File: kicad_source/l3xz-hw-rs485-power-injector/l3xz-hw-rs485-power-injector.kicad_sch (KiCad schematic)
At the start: 24 parts, among them J1 PowerPole, J2 Conn_01x02, J3 Conn_01x03, J4 SM04B-GHS-TB, J5 EH_S4B-EH, J6 EH_S4B-EH, J7 Conn_01x04, U1 L78L05_SOT89, U2 SN75176AD

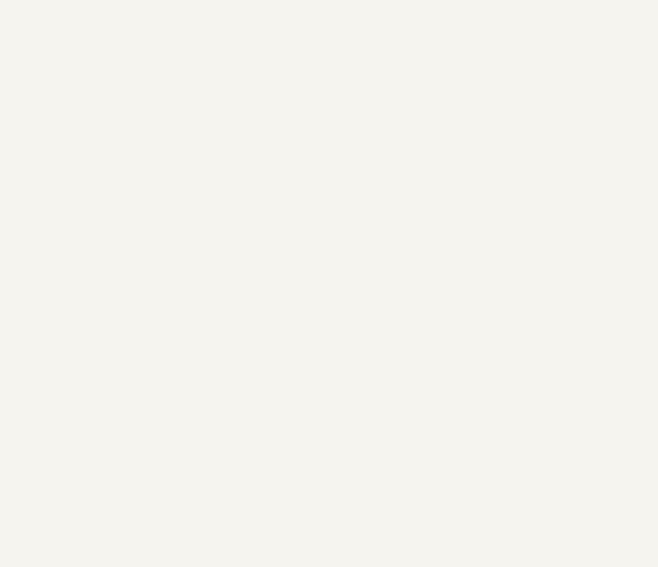
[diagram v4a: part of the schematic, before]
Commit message: added some labels
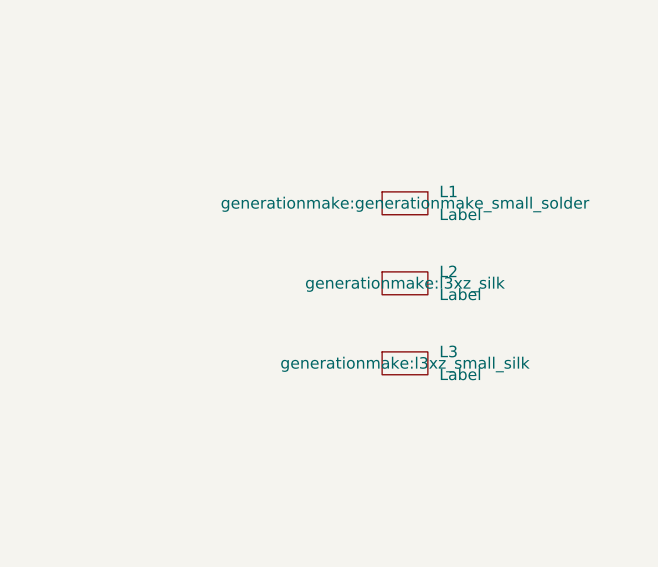
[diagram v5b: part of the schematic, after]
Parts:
- added L1: Label, generationmake:generationmake_small_solder, symbol generationmake:Label
- added L2: Label, generationmake:l3xz_silk, symbol generationmake:Label
- added L3: Label, generationmake:l3xz_small_silk, symbol generationmake:Label
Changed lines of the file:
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@@
     (pin "4")
+  )
+  (symbol (lib_id "generationmake:Label") (at 220.98 161.29 0) (unit 1)
+    (in_bom yes) (on_board yes) (fields_autoplaced)
+    (property "Reference" "L3" (id 0) (at 224.79 160.0199 0)
+      (effects (font (size 1.27 1.27)) (justify left))
+    )
+    (property "Value" "Label" (id 1) (at 224.79 162.5599 0)
+      (effects (font (size 1.27 1.27)) (justify left))
+    )
+    (property "Footprint" "generationmake:l3xz_small_silk" (id 2) (at 220.98 161.29 0))
+    (property "Datasheet" "" (id 3) (at 220.98 161.29 0)
+      (effects (font (size 1.27 1.27)) hide)
+    )
   )
   (symbol (lib_id "Interface_UART:SN75176AD") (at 115.57 160.02 0) (unit 1)
@@
     (pin "1")
   )
+  (symbol (lib_id "generationmake:Label") (at 220.98 152.4 0) (unit 1)
+    (in_bom yes) (on_board yes) (fields_autoplaced)
+    (property "Reference" "L2" (id 0) (at 224.79 151.1299 0)
+      (effects (font (size 1.27 1.27)) (justify left))
+    )
+    (property "Value" "Label" (id 1) (at 224.79 153.6699 0)
+      (effects (font (size 1.27 1.27)) (justify left))
+    )
+    (property "Footprint" "generationmake:l3xz_silk" (id 2) (at 220.98 152.4 0))
+    (property "Datasheet" "" (id 3) (at 220.98 152.4 0)
+      (effects (font (size 1.27 1.27)) hide)
+    )
+  )
   (symbol (lib_id "Device:C_Polarized") (at 100.33 91.44 0) (unit 1)
     (in_bom yes) (on_board yes) (fields_autoplaced)
@@
     )
     (pin "1")
+  )
+  (symbol (lib_id "generationmake:Label") (at 220.98 143.51 0) (unit 1)
+    (in_bom yes) (on_board yes) (fields_autoplaced)
+    (property "Reference" "L1" (id 0) (at 224.79 142.2399 0)
+      (effects (font (size 1.27 1.27)) (justify left))
+    )
+    (property "Value" "Label" (id 1) (at 224.79 144.7799 0)
+      (effects (font (size 1.27 1.27)) (justify left))
+    )
+    (property "Footprint" "generationmake:generationmake_small_solder" (id 2) (at 220.98 143.51 0))
+    (property "Datasheet" "" (id 3) (at 220.98 143.51 0)
+      (effects (font (size 1.27 1.27)) hide)
+    )
   )
   (symbol (lib_id "power:+BATT") (at 62.23 134.62 0) (unit 1)
@@
       (reference "J7") (unit 1) (value "Conn_01x04") (footprint "Connector_PinHeader_2.54mm:PinHeader_1x04_P2.54mm_Vertical")
     )
+    (path "/70777226-db48-4e47-af4f-24cdf1be9e26"
+      (reference "L1") (unit 1) (value "Label") (footprint "generationmake:generationmake_small_solder")
+    )
+    (path "/67c03991-fb90-4020-88f4-cc1f78c8a305"
+      (reference "L2") (unit 1) (value "Label") (footprint "generationmake:l3xz_silk")
+    )
+    (path "/488632c7-5f7a-471c-803a-f79bff4377f3"
+      (reference "L3") (unit 1) (value "Label") (footprint "generationmake:l3xz_small_silk")
+    )
     (path "/d10997a4-c66c-4c0c-b0e2-7abe2be8864b"

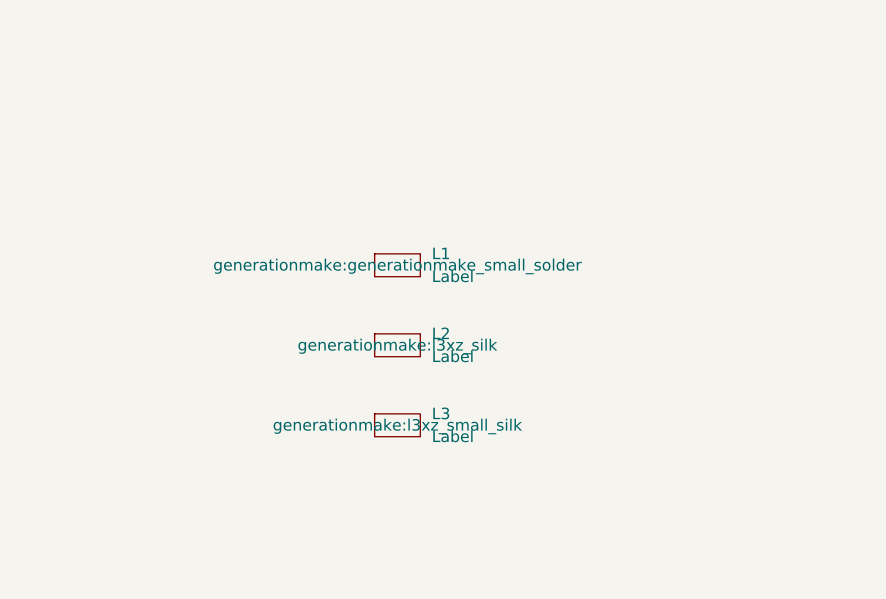
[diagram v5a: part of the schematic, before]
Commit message: added some labels
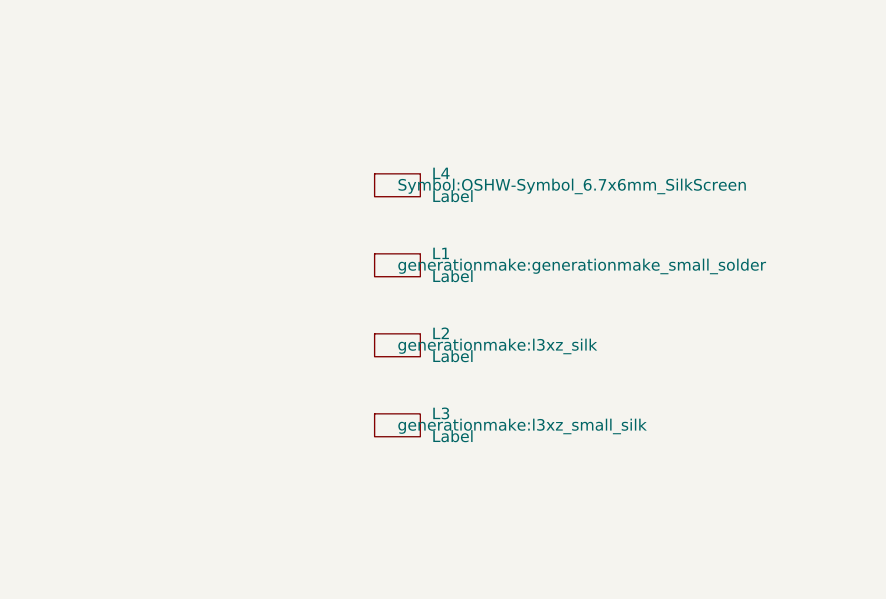
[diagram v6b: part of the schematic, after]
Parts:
- added L4: Label, Symbol:OSHW-Symbol_6.7x6mm_SilkScreen, symbol generationmake:Label
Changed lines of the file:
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@@
   (title_block
     (title "l3xz-hw-rs485-power-injector")
-    (date "2023-01-21")
+    (date "2023-01-23")
     (rev "0.1")
     (company "107-systems")
@@
       (effects (font (size 1.27 1.27)) (justify left))
     )
-    (property "Footprint" "generationmake:l3xz_small_silk" (id 2) (at 220.98 161.29 0))
+    (property "Footprint" "generationmake:l3xz_small_silk" (id 2) (at 220.98 161.29 0)
+      (effects (font (size 1.27 1.27)) (justify left))
+    )
     (property "Datasheet" "" (id 3) (at 220.98 161.29 0)
       (effects (font (size 1.27 1.27)) hide)
@@
     (pin "1")
   )
+  (symbol (lib_id "generationmake:Label") (at 220.98 134.62 0) (unit 1)
+    (in_bom yes) (on_board yes) (fields_autoplaced)
+    (property "Reference" "L4" (id 0) (at 224.79 133.3499 0)
+      (effects (font (size 1.27 1.27)) (justify left))
+    )
+    (property "Value" "Label" (id 1) (at 224.79 135.8899 0)
+      (effects (font (size 1.27 1.27)) (justify left))
+    )
+    (property "Footprint" "Symbol:OSHW-Symbol_6.7x6mm_SilkScreen" (id 2) (at 220.98 134.62 0)
+      (effects (font (size 1.27 1.27)) (justify left))
+    )
+    (property "Datasheet" "" (id 3) (at 220.98 134.62 0)
+      (effects (font (size 1.27 1.27)) hide)
+    )
+  )
   (symbol (lib_id "power:GND") (at 157.48 76.2 0) (mirror y) (unit 1)
     (in_bom yes) (on_board yes) (fields_autoplaced)
@@
       (effects (font (size 1.27 1.27)) (justify left))
     )
-    (property "Footprint" "generationmake:l3xz_silk" (id 2) (at 220.98 152.4 0))
+    (property "Footprint" "generationmake:l3xz_silk" (id 2) (at 220.98 152.4 0)
+      (effects (font (size 1.27 1.27)) (justify left))
+    )
     (property "Datasheet" "" (id 3) (at 220.98 152.4 0)
       (effects (font (size 1.27 1.27)) hide)
@@
       (effects (font (size 1.27 1.27)) (justify left))
     )
-    (property "Footprint" "generationmake:generationmake_small_solder" (id 2) (at 220.98 143.51 0))
+    (property "Footprint" "generationmake:generationmake_small_solder" (id 2) (at 220.98 143.51 0)
+      (effects (font (size 1.27 1.27)) (justify left))
+    )
     (property "Datasheet" "" (id 3) (at 220.98 143.51 0)
       (effects (font (size 1.27 1.27)) hide)
@@
       (reference "L3") (unit 1) (value "Label") (footprint "generationmake:l3xz_small_silk")
     )
+    (path "/596febd3-735f-46f0-9b2c-645cbbeb4795"
+      (reference "L4") (unit 1) (value "Label") (footprint "Symbol:OSHW-Symbol_6.7x6mm_SilkScreen")
+    )
     (path "/d10997a4-c66c-4c0c-b0e2-7abe2be8864b"

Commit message: generated BOM
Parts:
- J2: value Conn_01x02 -> DNI
- J3: value Conn_01x03 -> DNI
- J7: value Conn_01x04 -> DNI
- L1, L2, L3, L4: now left out of the parts list
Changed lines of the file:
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@@
     (in_bom yes) (on_board yes) (fields_autoplaced)
     (property "Reference" "J7" (id 0) (at 55.88 153.67 0))
-    (property "Value" "Conn_01x04" (id 1) (at 55.88 156.21 0))
+    (property "Value" "DNI" (id 1) (at 55.88 156.21 0))
     (property "Footprint" "Connector_PinHeader_2.54mm:PinHeader_1x04_P2.54mm_Vertical" (id 2) (at 55.88 162.56 0)
       (effects (font (size 1.27 1.27)) hide)
@@
   )
   (symbol (lib_id "generationmake:Label") (at 220.98 161.29 0) (unit 1)
-    (in_bom yes) (on_board yes) (fields_autoplaced)
+    (in_bom no) (on_board yes) (fields_autoplaced)
     (property "Reference" "L3" (id 0) (at 224.79 160.0199 0)
       (effects (font (size 1.27 1.27)) (justify left))
@@
     (in_bom yes) (on_board yes) (fields_autoplaced)
     (property "Reference" "J2" (id 0) (at 50.8 54.61 0))
-    (property "Value" "Conn_01x02" (id 1) (at 50.8 57.15 0))
+    (property "Value" "DNI" (id 1) (at 50.8 57.15 0))
     (property "Footprint" "Connector_Phoenix_MC:PhoenixContact_MC_1,5_2-G-3.5_1x02_P3.50mm_Horizontal" (id 2) (at 50.8 60.96 0)
       (effects (font (size 1.27 1.27)) hide)
@@
   )
   (symbol (lib_id "generationmake:Label") (at 220.98 134.62 0) (unit 1)
-    (in_bom yes) (on_board yes) (fields_autoplaced)
+    (in_bom no) (on_board yes) (fields_autoplaced)
     (property "Reference" "L4" (id 0) (at 224.79 133.3499 0)
       (effects (font (size 1.27 1.27)) (justify left))
@@
   )
   (symbol (lib_id "generationmake:Label") (at 220.98 152.4 0) (unit 1)
-    (in_bom yes) (on_board yes) (fields_autoplaced)
+    (in_bom no) (on_board yes) (fields_autoplaced)
     (property "Reference" "L2" (id 0) (at 224.79 151.1299 0)
       (effects (font (size 1.27 1.27)) (justify left))
@@
   )
   (symbol (lib_id "generationmake:Label") (at 220.98 143.51 0) (unit 1)
-    (in_bom yes) (on_board yes) (fields_autoplaced)
+    (in_bom no) (on_board yes) (fields_autoplaced)
     (property "Reference" "L1" (id 0) (at 224.79 142.2399 0)
       (effects (font (size 1.27 1.27)) (justify left))
@@
     (in_bom yes) (on_board yes) (fields_autoplaced)
     (property "Reference" "J3" (id 0) (at 52.07 78.74 0))
-    (property "Value" "Conn_01x03" (id 1) (at 52.07 81.28 0))
+    (property "Value" "DNI" (id 1) (at 52.07 81.28 0))
     (property "Footprint" "Connector_Phoenix_MC:PhoenixContact_MC_1,5_3-G-3.5_1x03_P3.50mm_Horizontal" (id 2) (at 52.07 87.63 0)
       (effects (font (size 1.27 1.27)) hide)
@@
     )
     (path "/52a8ea43-f624-436f-915f-cf8b98734f55"
-      (reference "J2") (unit 1) (value "Conn_01x02") (footprint "Connector_Phoenix_MC:PhoenixContact_MC_1,5_2-G-3.5_1x02_P3.50mm_Horizontal")
+      (reference "J2") (unit 1) (value "DNI") (footprint "Connector_Phoenix_MC:PhoenixContact_MC_1,5_2-G-3.5_1x02_P3.50mm_Horizontal")
     )
     (path "/c10ca67c-2bfd-4004-97ed-36a6e46014de"
-      (reference "J3") (unit 1) (value "Conn_01x03") (footprint "Connector_Phoenix_MC:PhoenixContact_MC_1,5_3-G-3.5_1x03_P3.50mm_Horizontal")
+      (reference "J3") (unit 1) (value "DNI") (footprint "Connector_Phoenix_MC:PhoenixContact_MC_1,5_3-G-3.5_1x03_P3.50mm_Horizontal")
     )
     (path "/5f34de6b-0e22-4f3c-89e9-d3cc7be38d5f"
@@
     )
     (path "/03f26ee5-8d2d-4291-a112-e75fe2ac42e3"
-      (reference "J7") (unit 1) (value "Conn_01x04") (footprint "Connector_PinHeader_2.54mm:PinHeader_1x04_P2.54mm_Vertical")
+      (reference "J7") (unit 1) (value "DNI") (footprint "Connector_PinHeader_2.54mm:PinHeader_1x04_P2.54mm_Vertical")
     )
     (path "/70777226-db48-4e47-af4f-24cdf1be9e26"
